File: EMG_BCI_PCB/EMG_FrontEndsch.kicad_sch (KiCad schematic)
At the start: 28 parts, among them U1 INA350, U1C TL072, U2 MCP1501-12xCH, U3 ADA4807-4

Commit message: More schematic changes
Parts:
- removed C1, C2, C5, C7: 4.7uF, Capacitor_SMD:C_0603_1608Metric_Pad1.05x0.95mm_HandSolder, symbol Device:C
- removed C3, C4: 0.1uF, Capacitor_SMD:C_0603_1608Metric_Pad1.05x0.95mm_HandSolder, symbol Device:C
- removed U1C: TL072, Package_SO:SOP-8_3.9x4.9mm_P1.27mm, symbol Amplifier_Operational:TL072
- removed U2: MCP1501-12xCH, Package_TO_SOT_SMD:SOT-23-6, symbol Reference_Voltage:MCP1501-12xCH
- added R2: 10k, Resistor_SMD:R_0805_2012Metric_Pad1.15x1.40mm_HandSolder, symbol Device:R
- added R3: 2k, Resistor_SMD:R_0805_2012Metric_Pad1.15x1.40mm_HandSolder, symbol Device:R
- added unit 4 of U2
- C11: value 330pF -> 0.0047u
- C12: value 3.3nF -> 0.01u
- R8: value 75.7K -> 56k
- R9: value 1.29M -> 36k
- renumbered U3 to U2
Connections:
- net +3.3V: now also R2.1
- net Earth: now also R3.2
- net at U1.5 (Ref): now also U2.13 (-), U2.14
- new net: R2.2, R3.1, U2.12 (+)
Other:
- moved on the sheet: C11, C13, C14, C15, C16, U3E

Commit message: Added power symbols for +/-3.3V
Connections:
- net +5V is gone; now on net +3.3V: C13.2, C15.2, C6.2, C8.2, U1.7 (Vs+), U3.4 (V+)
- net -5V renamed -3V3
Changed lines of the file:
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@@
 	(wire
 		(pts
-			(xy 118.11 24.13) (xy 118.11 26.67)
+			(xy 118.11 21.59) (xy 118.11 26.67)
 		)
 		(stroke
@@
 	(wire
 		(pts
-			(xy 80.01 154.94) (xy 80.01 146.05)
+			(xy 80.01 146.05) (xy 80.01 157.48)
 		)
 		(stroke
@@
 	(wire
 		(pts
-			(xy 80.01 118.11) (xy 80.01 120.65)
+			(xy 80.01 116.84) (xy 80.01 120.65)
 		)
 		(stroke
@@
 		)
 	)
-	(global_label "+5V"
-		(shape input)
-		(at 80.01 118.11 90)
-		(effects
-			(font
-				(size 1.27 1.27)
-			)
-			(justify left)
-		)
-		(property "Intersheetrefs" "${INTERSHEET_REFS}"
-			(at 80.01 118.11 0)
-			(effects
-				(font
-					(size 1.27 1.27)
-				)
-				(hide yes)
-			)
-		)
-	)
-	(global_label "-5V"
-		(shape input)
-		(at 80.01 154.94 270)
-		(effects
-			(font
-				(size 1.27 1.27)
-			)
-			(justify right)
-		)
-		(property "Intersheetrefs" "${INTERSHEET_REFS}"
-			(at 80.01 154.94 0)
-			(effects
-				(font
-					(size 1.27 1.27)
-				)
-				(hide yes)
-			)
-		)
-	)
 	(hierarchical_label "Electrode-"
 		(shape input)
@@
 	)
 	(symbol
-		(lib_id "power:+5V")
-		(at 118.11 24.13 0)
-		(unit 1)
-		(exclude_from_sim no)
-		(in_bom yes)
-		(on_board yes)
-		(dnp no)
-		(property "Reference" "#PWR0101"
-			(at 118.11 27.94 0)
-			(effects
-				(font
-					(size 1.27 1.27)
-				)
-				(hide yes)
-			)
-		)
-		(property "Value" "+5V"
-			(at 118.491 19.7358 0)
-			(effects
-				(font
-					(size 1.27 1.27)
-				)
-			)
-		)
-		(property "Footprint" ""
-			(at 118.11 24.13 0)
-			(effects
-				(font
-					(size 1.27 1.27)
-				)
-				(hide yes)
-			)
-		)
-		(property "Datasheet" ""
-			(at 118.11 24.13 0)
-			(effects
-				(font
-					(size 1.27 1.27)
-				)
-				(hide yes)
-			)
-		)
-		(property "Description" ""
-			(at 118.11 24.13 0)
-			(effects
-				(font
-					(size 1.27 1.27)
-				)
-			)
-		)
-		(pin "1"
-		)
-		(instances
-			(project "EMG_BCI_PCB"
-				(path "/55cf2478-b5ba-45ce-afa6-3f75a1bb5fb4/00000000-0000-0000-0000-00005f08a48b"
-					(reference "#PWR0101")
-					(unit 1)
-				)
-			)
-		)
-	)
-	(symbol
 		(lib_id "EMG_Circuit:ADA4807-4")
 		(at 87.63 83.82 0)
@@
 	)
 	(symbol
+		(lib_id "power:+3.3V")
+		(at 118.11 21.59 0)
+		(unit 1)
+		(exclude_from_sim no)
+		(in_bom yes)
+		(on_board yes)
+		(dnp no)
+		(fields_autoplaced yes)
+		(property "Reference" "#PWR032"
+			(at 118.11 25.4 0)
+			(effects
+				(font
+					(size 1.27 1.27)
+				)
+				(hide yes)
+			)
+		)
+		(property "Value" "+3.3V"
+			(at 118.11 16.51 0)
+			(effects
+				(font
+					(size 1.27 1.27)
+				)
+			)
+		)
+		(property "Footprint" ""
+			(at 118.11 21.59 0)
+			(effects
+				(font
+					(size 1.27 1.27)
+				)
+				(hide yes)
+			)
+		)
+		(property "Datasheet" ""
+			(at 118.11 21.59 0)
+			(effects
+				(font
+					(size 1.27 1.27)
+				)
+				(hide yes)
+			)
+		)
+		(property "Description" "Power symbol creates a global label with name \"+3.3V\""
+			(at 118.11 21.59 0)
+			(effects
+				(font
+					(size 1.27 1.27)
+				)
+				(hide yes)
+			)
+		)
+		(pin "1"
+		)
+		(instances
+			(project "EMG_BCI_PCB"
+				(path "/55cf2478-b5ba-45ce-afa6-3f75a1bb5fb4/00000000-0000-0000-0000-00005f08a48b"
+					(reference "#PWR032")
+					(unit 1)
+				)
+			)
+		)
+	)
+	(symbol
 		(lib_id "power:Earth")
 		(at 60.96 100.33 0)
@@
 	)
 	(symbol
+		(lib_id "power:-3V3")
+		(at 80.01 157.48 180)
+		(unit 1)
+		(exclude_from_sim no)
+		(in_bom yes)
+		(on_board yes)
+		(dnp no)
+		(fields_autoplaced yes)
+		(property "Reference" "#PWR040"
+			(at 80.01 153.67 0)
+			(effects
+				(font
+					(size 1.27 1.27)
+				)
+				(hide yes)
+			)
+		)
+		(property "Value" "-3V3"
+			(at 80.01 162.56 0)
+			(effects
+				(font
+					(size 1.27 1.27)
+				)
+			)
+		)
+		(property "Footprint" ""
+			(at 80.01 157.48 0)
+			(effects
+				(font
+					(size 1.27 1.27)
+				)
+				(hide yes)
+			)
+		)
+		(property "Datasheet" ""
+			(at 80.01 157.48 0)
+			(effects
+				(font
+					(size 1.27 1.27)
+				)
+				(hide yes)
+			)
+		)
+		(property "Description" "Power symbol creates a global label with name \"-3V3\""
+			(at 80.01 157.48 0)
+			(effects
+				(font
+					(size 1.27 1.27)
+				)
+				(hide yes)
+			)
+		)
+		(pin "1"
+		)
+		(instances
+			(project "EMG_BCI_PCB"
+				(path "/55cf2478-b5ba-45ce-afa6-3f75a1bb5fb4/00000000-0000-0000-0000-00005f08a48b"
+					(reference "#PWR040")
+					(unit 1)
+				)
+			)
+		)
+	)
+	(symbol
 		(lib_id "Device:R")
 		(at 60.96 90.17 0)
@@
 					(unit 1)
 				)
+			)
+		)
+	)
+	(symbol
+		(lib_id "power:+3.3V")
+		(at 80.01 116.84 0)
+		(unit 1)
+		(exclude_from_sim no)
+		(in_bom yes)
+		(on_board yes)
+		(dnp no)
+		(fields_autoplaced yes)
+		(property "Reference" "#PWR036"
+			(at 80.01 120.65 0)
+			(effects
+				(font
+					(size 1.27 1.27)
+				)
+				(hide yes)
+			)
+		)
+		(property "Value" "+3.3V"
+			(at 80.01 111.76 0)
+			(effects
+				(font
+					(size 1.27 1.27)
+				)
+			)
+		)
+		(property "Footprint" ""
+			(at 80.01 116.84 0)
+			(effects
+				(font
+					(size 1.27 1.27)
+				)
+				(hide yes)
+			)
+		)
+		(property "Datasheet" ""
+			(at 80.01 116.84 0)
+			(effects
+				(font
+					(size 1.27 1.27)
+				)
+				(hide yes)
+			)
+		)
+		(property "Description" "Power symbol creates a global label with name \"+3.3V\""
+			(at 80.01 116.84 0)
+			(effects
+				(font
+					(size 1.27 1.27)
+				)
+				(hide yes)
+			)
+		)
+		(pin "1"
+		)
+		(instances
+			(project "EMG_BCI_PCB"
+				(path "/55cf2478-b5ba-45ce-afa6-3f75a1bb5fb4/00000000-0000-0000-0000-00005f08a48b"
+					(reference "#PWR036")
+					(unit 1)
+				)

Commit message: Removed some warnings from the electrical rules
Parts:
- removed U2, U3: ADA4807-4, Package_SO:TSSOP-14_4.4x5mm_P0.65mm, symbol EMG_Circuit:ADA4807-4
- added U2: ADA4807-4ARUZ, Package_SO:TSSOP-14_4.4x5mm_P0.65mm, symbol Amplifier_Operational:ADA4807-4ARUZ
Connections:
- net +3.3V: now also U2.4 (V+)
- net -3V3: now also U2.11 (V-)
- net LP_OUT: now also U2.13 (-), U2.14
- net at R11.1: now also U2.1, U2.2 (-), U2.5 (+)
- net at C10.1, R10.1: now also U2.3 (+)
- net at R1.2, R12.1: now also U2.6 (-)
- net at R1.1, R8.2, TP2.1: now also U2.7
- net at C11.2, R9.1: now also U2.12 (+)
- net at R2.2, R3.1: now also U2.10 (+)
- net at U1.5 (Ref): now also U2.8, U2.9 (-)

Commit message: Assigned footprints to components
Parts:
- C10, C11, C12, C13, C14, C15, C16, C6, C8, C9: footprint Capacitor_SMD:C_0603_1608Metric_Pad1.05x0.95mm_HandSolder -> Capacitor_SMD:C_0201_0603Metric_Pad0.64x0.40mm_HandSolder
- R1, R10, R11, R12, R2, R3, R8, R9: footprint Resistor_SMD:R_0805_2012Metric_Pad1.15x1.40mm_HandSolder -> Resistor_SMD:R_0603_1608Metric_Pad0.98x0.95mm_HandSolder
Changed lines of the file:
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@@
 			)
 		)
-		(property "Footprint" "Capacitor_SMD:C_0603_1608Metric_Pad1.05x0.95mm_HandSolder"
+		(property "Footprint" "Capacitor_SMD:C_0201_0603Metric_Pad0.64x0.40mm_HandSolder"
 			(at 137.16 55.5752 0)
 			(effects
@@
 			)
 		)
-		(property "Footprint" "Capacitor_SMD:C_0603_1608Metric_Pad1.05x0.95mm_HandSolder"
+		(property "Footprint" "Capacitor_SMD:C_0201_0603Metric_Pad0.64x0.40mm_HandSolder"
 			(at 152.4 55.5752 0)
 			(effects
@@
 			)
 		)
-		(property "Footprint" "Resistor_SMD:R_0805_2012Metric_Pad1.15x1.40mm_HandSolder"
+		(property "Footprint" "Resistor_SMD:R_0603_1608Metric_Pad0.98x0.95mm_HandSolder"
 			(at 167.132 60.96 90)
 			(effects
@@
 			)
 		)
-		(property "Footprint" "Resistor_SMD:R_0805_2012Metric_Pad1.15x1.40mm_HandSolder"
+		(property "Footprint" "Resistor_SMD:R_0603_1608Metric_Pad0.98x0.95mm_HandSolder"
 			(at 253.492 80.01 90)
 			(effects
@@
 			)
 		)
-		(property "Footprint" "Capacitor_SMD:C_0603_1608Metric_Pad1.05x0.95mm_HandSolder"
+		(property "Footprint" "Capacitor_SMD:C_0201_0603Metric_Pad0.64x0.40mm_HandSolder"
 			(at 160.3248 111.76 0)
 			(effects
@@
 			)
 		)
-		(property "Footprint" "Capacitor_SMD:C_0603_1608Metric_Pad1.05x0.95mm_HandSolder"
+		(property "Footprint" "Capacitor_SMD:C_0201_0603Metric_Pad0.64x0.40mm_HandSolder"
 			(at 187.96 131.1148 0)
 			(effects
@@
 			)
 		)
-		(property "Footprint" "Resistor_SMD:R_0805_2012Metric_Pad1.15x1.40mm_HandSolder"
+		(property "Footprint" "Resistor_SMD:R_0603_1608Metric_Pad0.98x0.95mm_HandSolder"
 			(at 168.91 78.232 90)
 			(effects
@@
 			)
 		)
-		(property "Footprint" "Resistor_SMD:R_0805_2012Metric_Pad1.15x1.40mm_HandSolder"
+		(property "Footprint" "Resistor_SMD:R_0603_1608Metric_Pad0.98x0.95mm_HandSolder"
 			(at 134.62 107.442 90)
 			(effects
@@
 			)
 		)
-		(property "Footprint" "Resistor_SMD:R_0805_2012Metric_Pad1.15x1.40mm_HandSolder"
+		(property "Footprint" "Resistor_SMD:R_0603_1608Metric_Pad0.98x0.95mm_HandSolder"
 			(at 152.4 107.442 90)
 			(effects
@@
 			)
 		)
-		(property "Footprint" "Capacitor_SMD:C_0603_1608Metric_Pad1.05x0.95mm_HandSolder"
+		(property "Footprint" "Capacitor_SMD:C_0201_0603Metric_Pad0.64x0.40mm_HandSolder"
 			(at 124.7648 27.94 0)
 			(effects
@@
 			)
 		)
-		(property "Footprint" "Capacitor_SMD:C_0603_1608Metric_Pad1.05x0.95mm_HandSolder"
+		(property "Footprint" "Capacitor_SMD:C_0201_0603Metric_Pad0.64x0.40mm_HandSolder"
 			(at 137.4648 27.94 0)
 			(effects
@@
 			)
 		)
-		(property "Footprint" "Capacitor_SMD:C_0603_1608Metric_Pad1.05x0.95mm_HandSolder"
+		(property "Footprint" "Capacitor_SMD:C_0201_0603Metric_Pad0.64x0.40mm_HandSolder"
 			(at 95.5548 121.92 0)
 			(effects
@@
 			)
 		)
-		(property "Footprint" "Capacitor_SMD:C_0603_1608Metric_Pad1.05x0.95mm_HandSolder"
+		(property "Footprint" "Capacitor_SMD:C_0201_0603Metric_Pad0.64x0.40mm_HandSolder"
 			(at 106.9848 121.92 0)
 			(effects
@@
 			)
 		)
-		(property "Footprint" "Capacitor_SMD:C_0603_1608Metric_Pad1.05x0.95mm_HandSolder"
+		(property "Footprint" "Capacitor_SMD:C_0201_0603Metric_Pad0.64x0.40mm_HandSolder"
 			(at 95.5548 147.32 0)
 			(effects
@@
 			)
 		)
-		(property "Footprint" "Capacitor_SMD:C_0603_1608Metric_Pad1.05x0.95mm_HandSolder"
+		(property "Footprint" "Capacitor_SMD:C_0201_0603Metric_Pad0.64x0.40mm_HandSolder"
 			(at 106.9848 147.32 0)
 			(effects
@@
 			)
 		)
-		(property "Footprint" "Resistor_SMD:R_0805_2012Metric_Pad1.15x1.40mm_HandSolder"
+		(property "Footprint" "Resistor_SMD:R_0603_1608Metric_Pad0.98x0.95mm_HandSolder"
 			(at 253.492 69.85 90)
 			(effects
@@
 			)
 		)
-		(property "Footprint" "Resistor_SMD:R_0805_2012Metric_Pad1.15x1.40mm_HandSolder"
+		(property "Footprint" "Resistor_SMD:R_0603_1608Metric_Pad0.98x0.95mm_HandSolder"
 			(at 59.182 90.17 90)
 			(effects
@@
 			)
 		)
-		(property "Footprint" "Resistor_SMD:R_0805_2012Metric_Pad1.15x1.40mm_HandSolder"
+		(property "Footprint" "Resistor_SMD:R_0603_1608Metric_Pad0.98x0.95mm_HandSolder"
 			(at 59.182 73.66 90)
 			(effects

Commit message: finally assigned the footprints to the schematic symbols
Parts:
- U1: footprint (none) -> Wills_FootprintLibrary:SOT-23-THIN
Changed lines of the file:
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@@
 			)
 		)
-		(property "Footprint" ""
+		(property "Footprint" "Wills_FootprintLibrary:SOT-23-THIN"
 			(at 118.11 54.61 0)
 			(effects

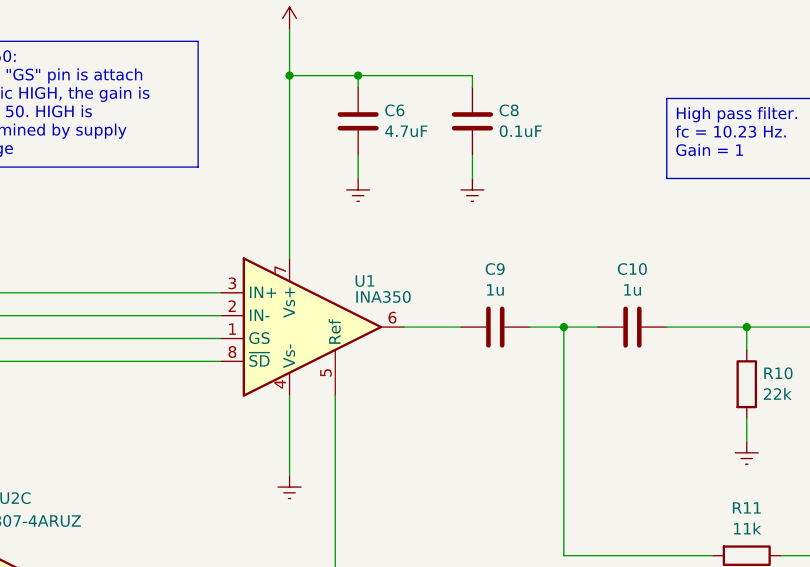
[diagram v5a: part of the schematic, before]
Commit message: Ran ERC again
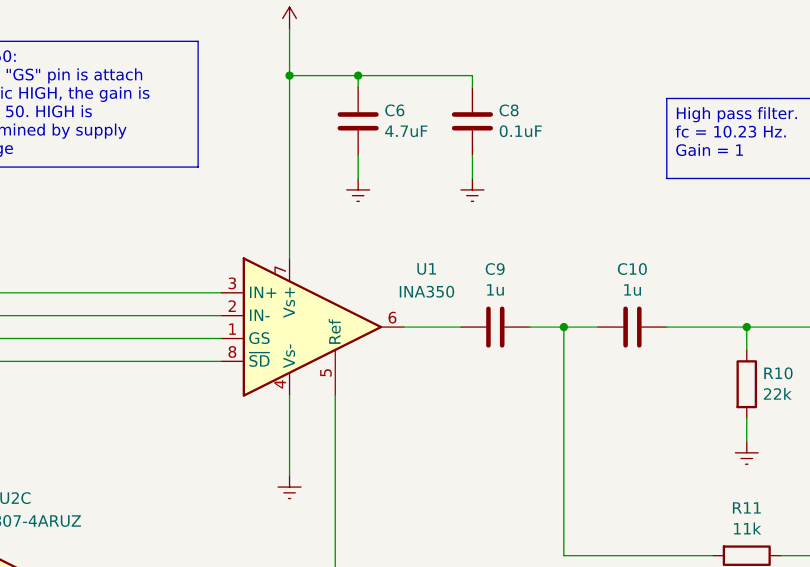
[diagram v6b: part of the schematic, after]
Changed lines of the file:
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@@
+	)
+	(symbol
+		(lib_id "WillsLibrary:INA350")
+		(at 118.11 54.61 0)
+		(unit 1)
+		(exclude_from_sim no)
+		(in_bom yes)
+		(on_board yes)
+		(dnp no)
+		(fields_autoplaced yes)
+		(property "Reference" "U1"
+			(at 133.35 48.1898 0)
+			(effects
+				(font
+					(size 1.27 1.27)
+				)
+			)
+		)
+		(property "Value" "INA350"
+			(at 133.35 50.7298 0)
+			(effects
+				(font
+					(size 1.27 1.27)
+				)
+			)
+		)
+		(property "Footprint" "Wills_FootprintLibrary:SOT-23-THIN"
+			(at 118.11 54.61 0)
+			(effects
+				(font
+					(size 1.27 1.27)
+				)
+				(hide yes)
+			)
+		)
+		(property "Datasheet" ""
+			(at 118.11 54.61 0)
+			(effects
+				(font
+					(size 1.27 1.27)
+				)
+				(hide yes)
+			)
+		)
+		(property "Description" ""
+			(at 118.11 54.61 0)
+			(effects
+				(font
+					(size 1.27 1.27)
+				)
+				(hide yes)
+			)
+		)
+		(pin "1"
+		)
+		(pin "5"
+		)
+		(pin "7"
+		)
+		(pin "2"
+		)
+		(pin "4"
+		)
+		(pin "8"
+		)
+		(pin "3"
+		)
+		(pin "6"
+		)
+		(instances
+			(project ""
+				(path "/55cf2478-b5ba-45ce-afa6-3f75a1bb5fb4/00000000-0000-0000-0000-00005f08a48b"
+					(reference "U1")
+					(unit 1)
+				)
+			)
+		)
 	)
 	(symbol
@@
 					(unit 1)
 				)
-			)
-		)
-	)
-	(symbol
-		(lib_id "WillsLibrary:INA350")
-		(at 118.11 54.61 0)
-		(unit 1)
-		(exclude_from_sim no)
-		(in_bom yes)
-		(on_board yes)
-		(dnp no)
-		(property "Reference" "U1"
-			(at 126.492 49.53 0)
-			(effects
-				(font
-					(size 1.27 1.27)
-				)
-			)
-		)
-		(property "Value" "INA350"
-			(at 128.524 51.308 0)
-			(effects
-				(font
-					(size 1.27 1.27)
-				)
-			)
-		)
-		(property "Footprint" "Wills_FootprintLibrary:SOT-23-THIN"
-			(at 118.11 54.61 0)
-			(effects
-				(font
-					(size 1.27 1.27)
-				)
-				(hide yes)
-			)
-		)
-		(property "Datasheet" ""
-			(at 118.11 54.61 0)
-			(effects
-				(font
-					(size 1.27 1.27)
-				)
-				(hide yes)
-			)
-		)
-		(property "Description" ""
-			(at 118.11 54.61 0)
-			(effects
-				(font
-					(size 1.27 1.27)
-				)
-				(hide yes)
-			)
-		)
-		(pin "3"
-		)
-		(pin "1"
-		)
-		(pin "8"
-		)
-		(pin "7"
-		)
-		(pin "2"
-		)
-		(pin "4"
-		)
-		(pin "5"
-		)
-		(pin "6"
-		)
-		(instances
-			(project ""
-				(path "/55cf2478-b5ba-45ce-afa6-3f75a1bb5fb4/00000000-0000-0000-0000-00005f08a48b"
-					(reference "U1")
-					(unit 1)
-				)
